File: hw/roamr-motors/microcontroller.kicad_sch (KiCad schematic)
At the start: 1 part, among them U3 ESP32-S3-WROOM-1

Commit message: WIP ESP32 and USB UART
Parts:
- added C1, C2: 0.1uF, symbol Device:C
- added C3: 1uF, symbol Device:C
- added C4, C5, C6: 10uF, symbol Device:C
- added D1, D6: D, symbol Device:D
- added D2, D3, D4, D5, D7, D8: D_TVS, symbol Device:D_TVS
- added L1: L, symbol Device:L
- added P1, P2: USB_C_Plug_USB2.0, symbol Connector:USB_C_Plug_USB2.0
- added U4: CP2102N-Axx-xQFN28, Package_DFN_QFN:QFN-28-1EP_5x5mm_P0.5mm_EP3.35x3.35mm, symbol Interface_USB:CP2102N-Axx-xQFN28
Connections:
- net GND: now also C1.2, C2.2, C3.2, C4.2, C5.2, C6.2, D2.1 (A1), D3.1 (A1), D4.1 (A1), D5.1 (A1), D7.1 (A1), D8.1 (A1), P1.A1 (GND), P1.A12 (GND), P1.B1 (GND), P1.B12 (GND), P1.S1 (SHIELD), P2.A1 (GND), P2.A12 (GND), P2.B1 (GND), P2.B12 (GND), P2.S1 (SHIELD)
- net GPIO8_I_SENSE_R1: now reaches U3.12 (IO8)
- net GPIO19_USB_DN: now reaches U3.13 (USB_D-)
- net GPIO19_USB_DN: now also D7.2 (A2), P2.A7 (D-)
- net GPIO20_USB_DP: now reaches U3.14 (USB_D+)
- net GPIO20_USB_DP: now also D8.2 (A2), P2.A6 (D+)
- net GPIO9_I_SENSE_R2: now reaches U3.17 (IO9)
- net GPIO10_I_SENSE_R3: now reaches U3.18 (IO10)
- net at U3.2 (3V3): now also U3.3 (EN), C1.1, L1.2
- net GPIO5_I_SENSE_L1: now reaches U3.5 (IO5)
- net GPIO6_I_SENSE_L2: now reaches U3.6 (IO6)
- net GPIO7_I_SENSE_L3: now reaches U3.7 (IO7)
- new net: D5.2 (A2), D6.2 (A), P2.A4 (VBUS), P2.A9 (VBUS), P2.B4 (VBUS), P2.B9 (VBUS)
- new net: D1.2 (A), D4.2 (A2), P1.A4 (VBUS), P1.A9 (VBUS), P1.B4 (VBUS), P1.B9 (VBUS)
- new net: U4.29 (GND), U4.3 (GND)
- new net USB_DN: D3.2 (A2), P1.A7 (D-)
- new net USB_DP: D2.2 (A2), P1.A6 (D+)
- new net VDD3_3: C2.1, C3.1, C4.1, L1.1
- new net VDD5: C5.1, C6.1, D1.1 (K), D6.1 (K)
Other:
- moved on the sheet: U3

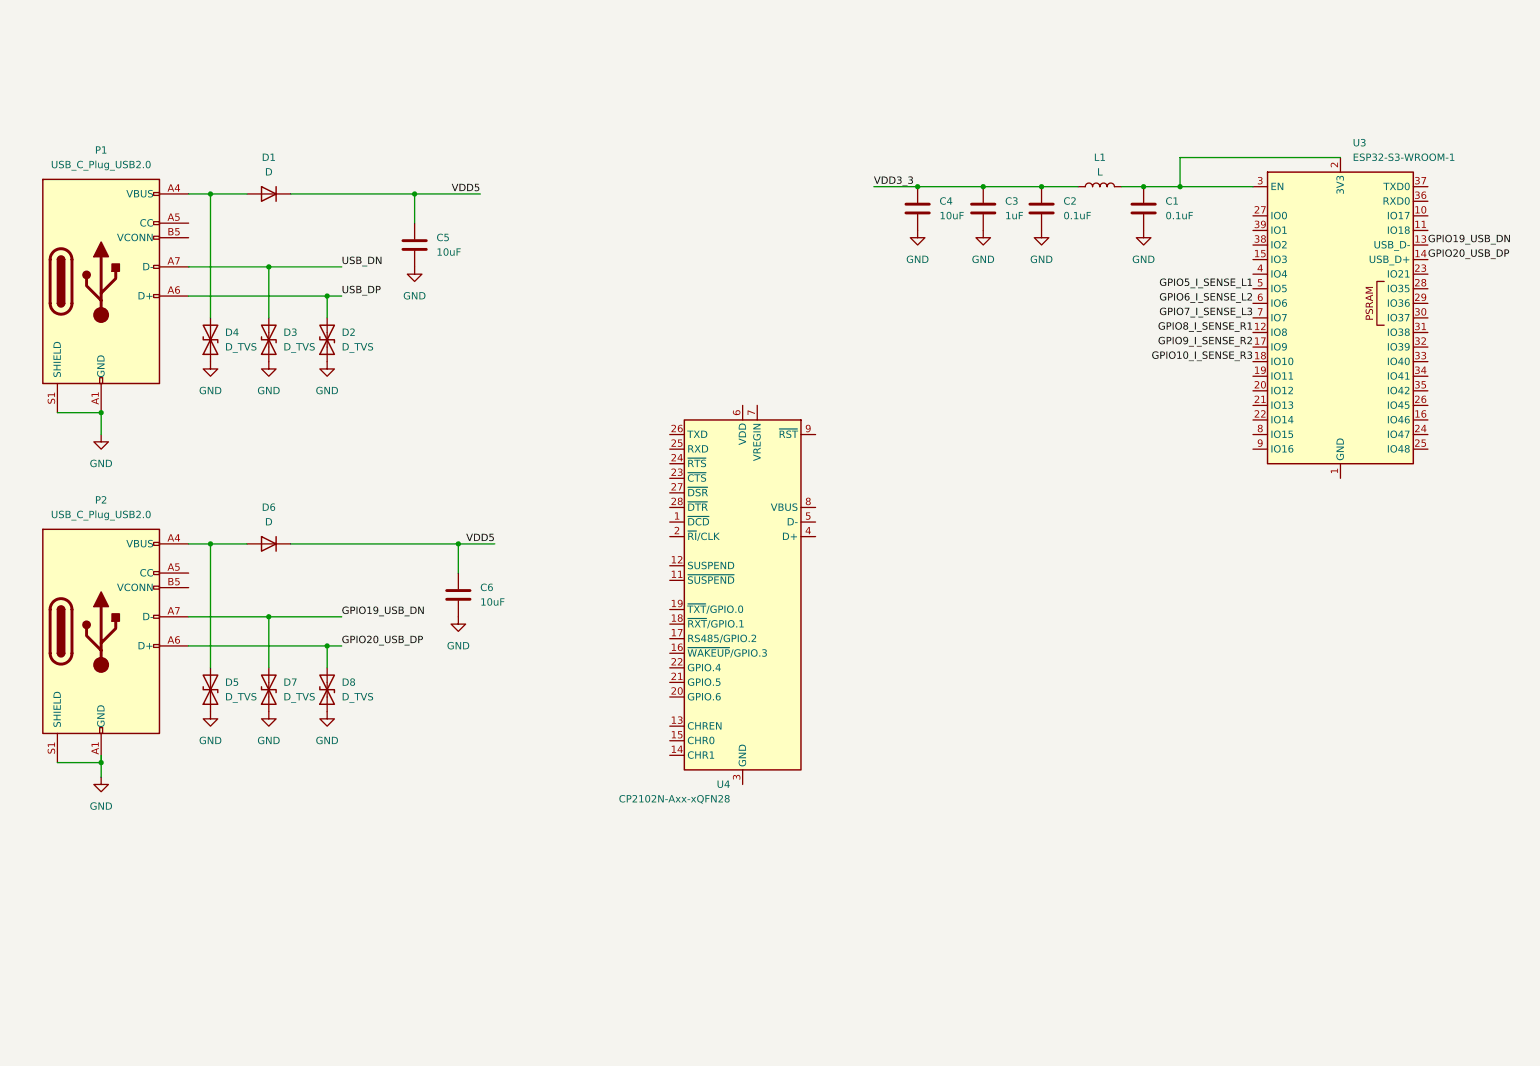
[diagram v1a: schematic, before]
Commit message: Add USB-UART, USB receptacles, ESP32-S3-WROOM-1, switches. TODO: 5V_3V3 LDO, BLDC drivers, encoder SPI, connectors
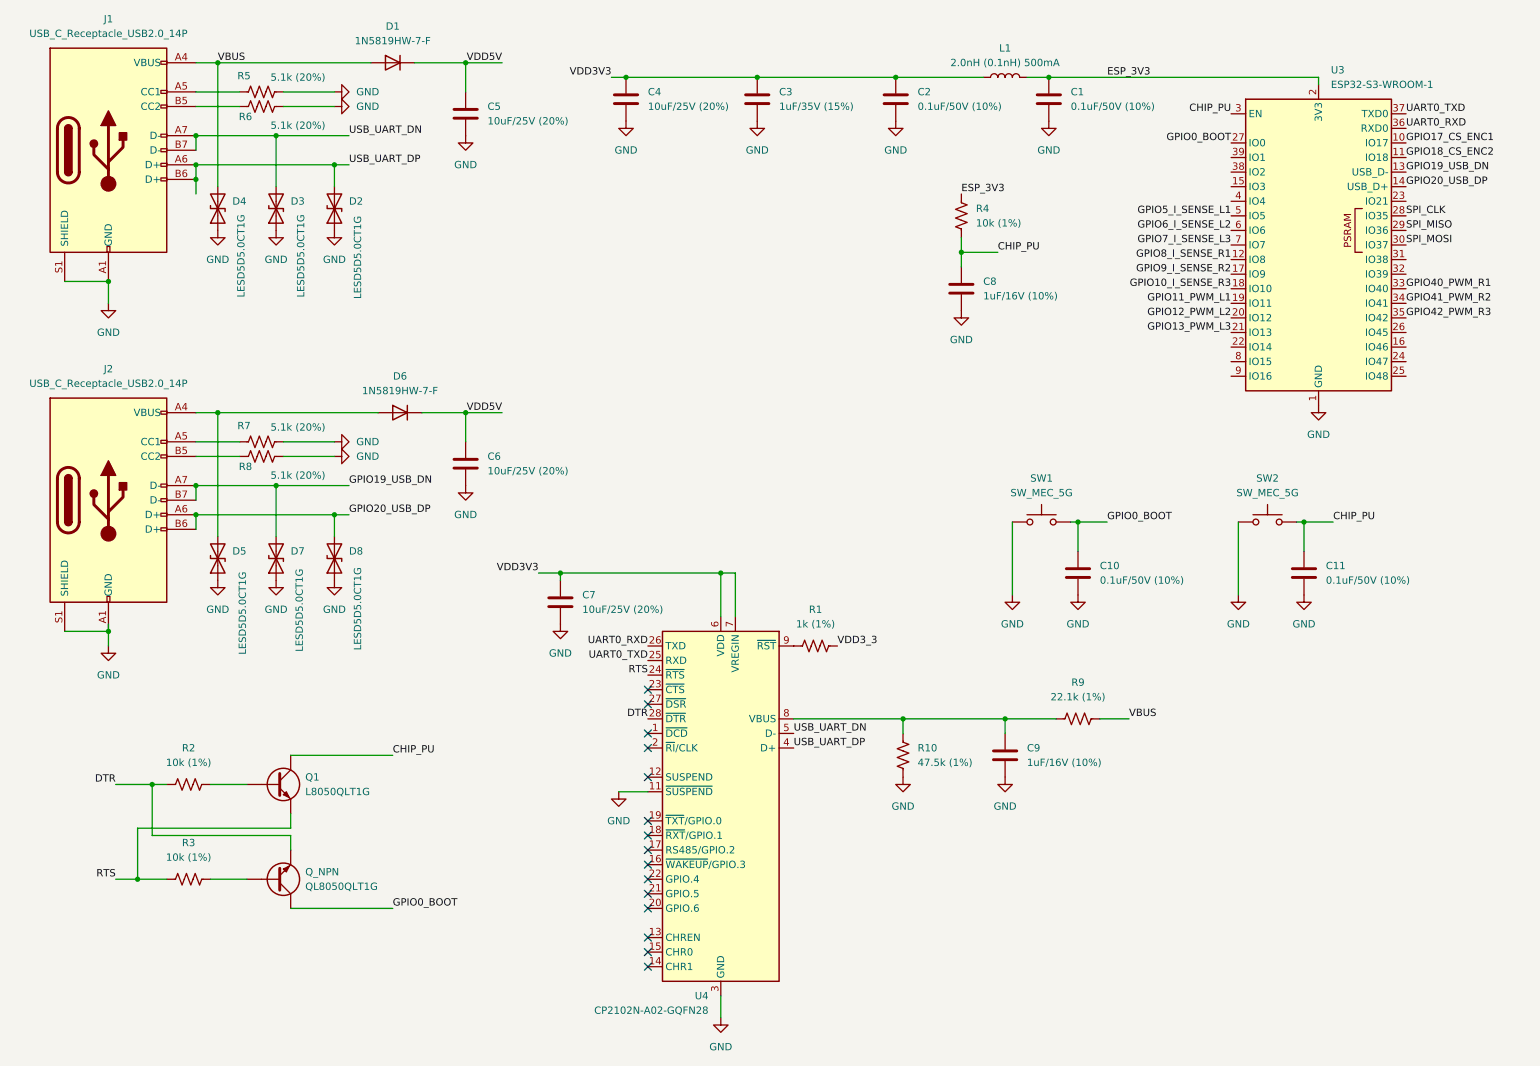
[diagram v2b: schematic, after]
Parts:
- removed P1, P2: USB_C_Plug_USB2.0, symbol Connector:USB_C_Plug_USB2.0
- added C10, C11: 0.1uF/50V (10%), symbol Device:C
- added C7: 10uF/25V (20%), symbol Device:C
- added C8, C9: 1uF/16V (10%), symbol Device:C
- added J1, J2: USB_C_Receptacle_USB2.0_14P, symbol Connector:USB_C_Receptacle_USB2.0_14P
- added Q1: L8050QLT1G, symbol Device:Q_NPN
- added QL8050QLT1G: Q_NPN, symbol Device:Q_NPN
- added R1: 1k (1%), symbol Device:R_US
- added R10: 47.5k (1%), symbol Device:R_US
- added R2, R3, R4: 10k (1%), symbol Device:R_US
- added R5, R6, R7, R8: 5.1k (20%), symbol Device:R_US
- added R9: 22.1k (1%), symbol Device:R_US
- added SW1, SW2: SW_MEC_5G, symbol Switch:SW_MEC_5G
- C1, C2: value 0.1uF -> 0.1uF/50V (10%)
- C3: value 1uF -> 1uF/35V (15%)
- C4, C5, C6: value 10uF -> 10uF/25V (20%)
- D1, D6: value D -> 1N5819HW-7-F
- D2, D3, D4, D5, D7, D8: value D_TVS -> LESD5D5.0CT1G
- L1: value L -> 2.0nH (0.1nH) 500mA
- U4: value CP2102N-Axx-xQFN28 -> CP2102N-A02-GQFN28
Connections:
- net USB_DN is gone; now on net USB_UART_DN: D3.2 (A2)
- net USB_DP is gone; now on net USB_UART_DP: D2.2 (A2)
- net GND: now also U3.1 (GND), U3.40 (GND), U3.41 (GND), U4.11 (~{SUSPEND}), U4.29 (GND), U4.3 (GND), C10.2, C11.2, C7.2, C8.2, C9.2, J1.A1 (GND), J1.A12 (GND), J1.B1 (GND), J1.B12 (GND), J1.S1 (SHIELD), J2.A1 (GND), J2.A12 (GND), J2.B1 (GND), J2.B12 (GND), J2.S1 (SHIELD), R10.1, R5.2, R6.2, R7.2, R8.2, SW1.1 (A), SW1.2 (A), SW2.1 (A), SW2.2 (A)
- net GPIO19_USB_DN: now also J2.A7 (D-), J2.B7 (D-)
- net GPIO20_USB_DP: now also J2.A6 (D+), J2.B6 (D+)
- net VDD3_3: now also R1.2; no longer C2.1, C3.1, C4.1, L1.1
- net at D5.2 (A2), D6.2 (A): now also J2.A4 (VBUS), J2.A9 (VBUS), J2.B4 (VBUS), J2.B9 (VBUS)
- net VBUS: now reaches D1.2 (A), D4.2 (A2)
- net VBUS: now also J1.A4 (VBUS), J1.A9 (VBUS), J1.B4 (VBUS), J1.B9 (VBUS), R9.2
- net RTS: now reaches U4.24 (~{RTS})
- net RTS: now also Q1.E, R3.1
- net UART0_TXD: now reaches U4.25 (RXD)
- net UART0_TXD: now also U3.37 (TXD0)
- net UART0_RXD: now reaches U4.26 (TXD)
- net UART0_RXD: now also U3.36 (RXD0)
- net DTR: now reaches U4.28 (~{DTR})
- net DTR: now also QL8050QLT1G.E, R2.1
- net USB_UART_DP: now reaches U4.4 (D+)
- net USB_UART_DP: now also J1.A6 (D+), J1.B6 (D+)
- net USB_UART_DN: now reaches U4.5 (D-)
- net USB_UART_DN: now also J1.A7 (D-), J1.B7 (D-)
- net VDD3V3: now reaches U4.6 (VDD)
- net VDD3V3: now also C2.1, C3.1, C4.1, L1.1, U4.7 (VREGIN), C7.1
- net at U4.8 (VBUS): now also C9.1, R10.2, R9.1
- net at U4.9 (~{RST}): now also R1.1
- net GPIO17_CS_ENC1: now reaches U3.10 (IO17)
- net GPIO18_CS_ENC2: now reaches U3.11 (IO18)
- net GPIO11_PWM_L1: now reaches U3.19 (IO11)
- net ESP_3V3: now reaches C1.1, L1.2, U3.2 (3V3)
- net ESP_3V3: now also R4.1; no longer U3.3 (EN)
- net GPIO12_PWM_L2: now reaches U3.20 (IO12)
- net GPIO13_PWM_L3: now reaches U3.21 (IO13)
- net GPIO0_BOOT: now reaches U3.27 (IO0)
- net GPIO0_BOOT: now also C10.1, QL8050QLT1G.C, SW1.3 (B), SW1.4 (B)
- net SPI_CLK: now reaches U3.28 (IO35)
- net SPI_MISO: now reaches U3.29 (IO36)
- net SPI_MOSI: now reaches U3.30 (IO37)
- net GPIO40_PWM_R1: now reaches U3.33 (IO40)
- net GPIO41_PWM_R2: now reaches U3.34 (IO41)
- net GPIO42_PWM_R3: now reaches U3.35 (IO42)
- net VDD5 renamed VDD5V
- new net: Q1.B, R2.2
- new net: QL8050QLT1G.B, R3.2
- new net: J1.A5 (CC1), R5.1
- new net: J2.B5 (CC2), R8.1
- new net: J2.A5 (CC1), R7.1
- new net: J1.B5 (CC2), R6.1
- new net CHIP_PU: C11.1, C8.1, Q1.C, R4.2, SW2.3 (B), SW2.4 (B), U3.3 (EN)
- no-connect marks 0 -> 15
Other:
- moved on the sheet: C1, C2, C3, C4, C5, C6, D1, D2, D3, D4, D5, D6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
